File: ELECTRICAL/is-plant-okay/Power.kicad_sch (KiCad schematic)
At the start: 0 parts

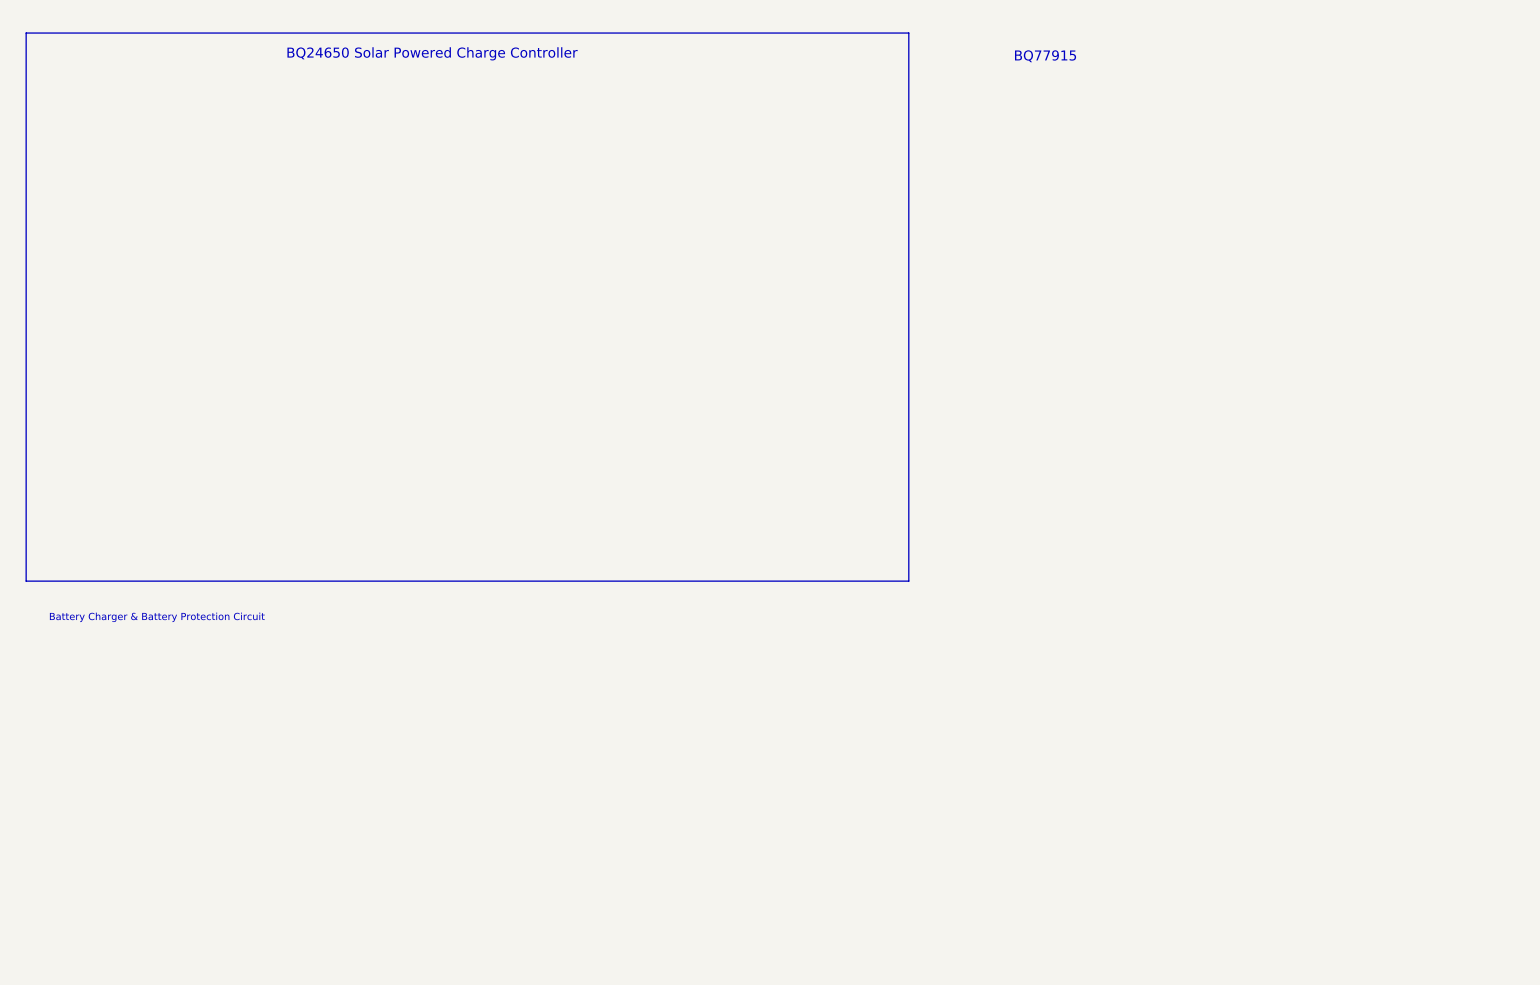
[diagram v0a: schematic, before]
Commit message: add bq24650 schematic
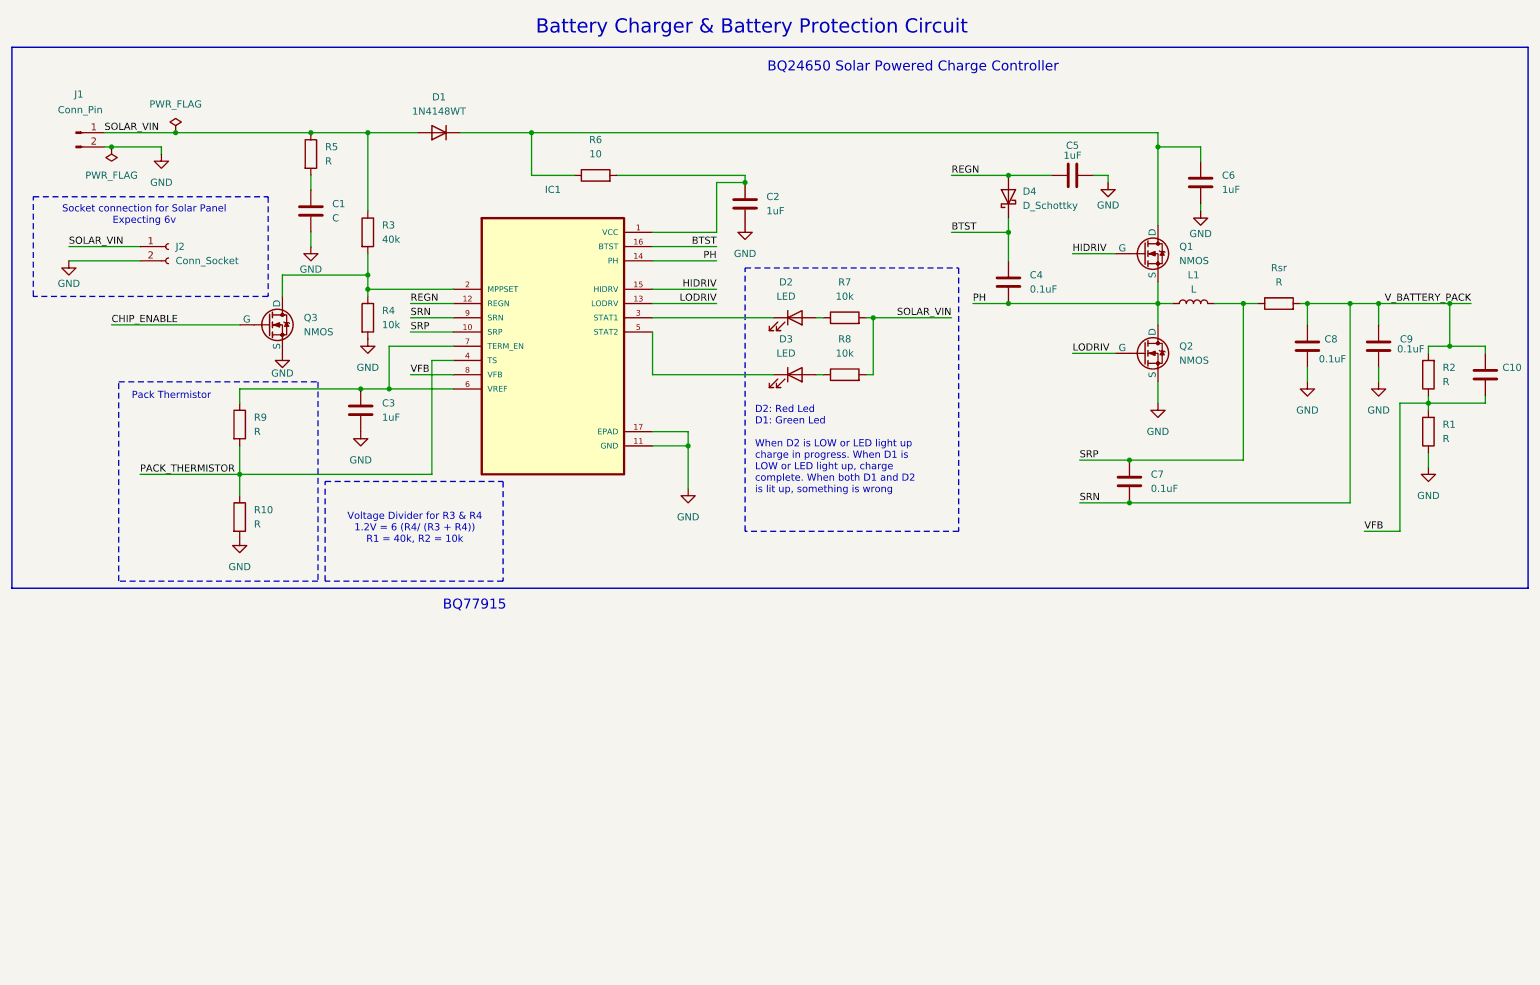
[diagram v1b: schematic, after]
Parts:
- added C1: C, symbol Device:C
- added C10: ~, symbol Device:C
- added C2, C3, C5, C6: 1uF, symbol Device:C
- added C4, C7, C8, C9: 0.1uF, symbol Device:C
- added D1: 1N4148WT, Diode_SMD:D_SOD-523, symbol Diode:1N4148WT
- added D2, D3: LED, symbol Device:LED
- added D4: D_Schottky, symbol Device:D_Schottky
- added IC1: ~, is-plant-okay-foot:QFN50P350X350X100-17N, symbol is-plant-okay-lib:BQ24650RVAT
- added J1: Conn_Pin, symbol Connector:Conn_01x02_Pin
- added J2: Conn_Socket, symbol Connector:Conn_01x02_Socket
- added L1: L, symbol Device:L
- added Q1, Q2, Q3: NMOS, symbol CustomLibrary:NMOS
- added R1, R10, R2, R5, R9, Rsr: R, symbol Device:R
- added R3: 40k, symbol Device:R
- added R4, R7, R8: 10k, symbol Device:R
- added R6: 10, symbol Device:R
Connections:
- new net: C6.1, D1.1 (K), Q1.1 (D), R6.1
- new net: C2.1, IC1.1 (VCC), R6.2
- new net: D3.2 (A), R8.1
- new net: D2.1 (K), IC1.3 (STAT1)
- new net: D2.2 (A), R7.1
- new net: IC1.2 (MPPSET), Q3.1 (D), R3.2, R4.1
- new net: D3.1 (K), IC1.5 (STAT2)
- new net: C3.1, IC1.6 (VREF), IC1.7 (TERM_EN), R9.1
- new net: C1.1, R5.2
- new net BTST: C4.1, D4.1 (K), IC1.16 (BTST)
- new net CHIP_ENABLE: Q3.2 (G)
- new net GND: C1.2, C2.2, C3.2, C5.2, C6.2, C8.2, C9.2, IC1.11 (GND), IC1.17 (EPAD), J1.2 (Pin_2), J2.2 (Pin_2), Q2.3 (S), Q3.3 (S), R1.1, R10.2, R4.2
- new net HIDRIV: IC1.15 (HIDRV), Q1.2 (G)
- new net LODRIV: IC1.13 (LODRV), Q2.2 (G)
- new net PACK_THERMISTOR: IC1.4 (TS), R10.1, R9.2
- new net PH: C4.2, IC1.14 (PH), L1.1, Q1.3 (S), Q2.1 (D)
- new net REGN: C5.1, D4.2 (A), IC1.12 (REGN)
- new net SOLAR_VIN: D1.2 (A), J1.1 (Pin_1), J2.1 (Pin_1), R3.1, R5.1, R7.2, R8.2
- new net SRN: C10.1, C7.2, C8.1, C9.1, IC1.9 (SRN), R2.2, Rsr.2
- new net SRP: C7.1, IC1.10 (SRP), L1.2, Rsr.1
- new net VFB: C10.2, IC1.8 (VFB), R1.2, R2.1
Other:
- note added: "D2: Red Led D1: Green Led When D2 is LOW or LED light up charge in progress. When D1 is LOW or LED light up, charge complete. When both D1 and D2 is lit up, something is wrong"
- note added: "Pack Thermistor"
- note added: "Socket connection for Solar Panel Expecting 6v"
- note added: "Voltage Divider for R3 & R4 1.2V = 6 (R4/ (R3 + R4)) R1 = 40k, R2 = 10k"

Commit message: add bq77915 module
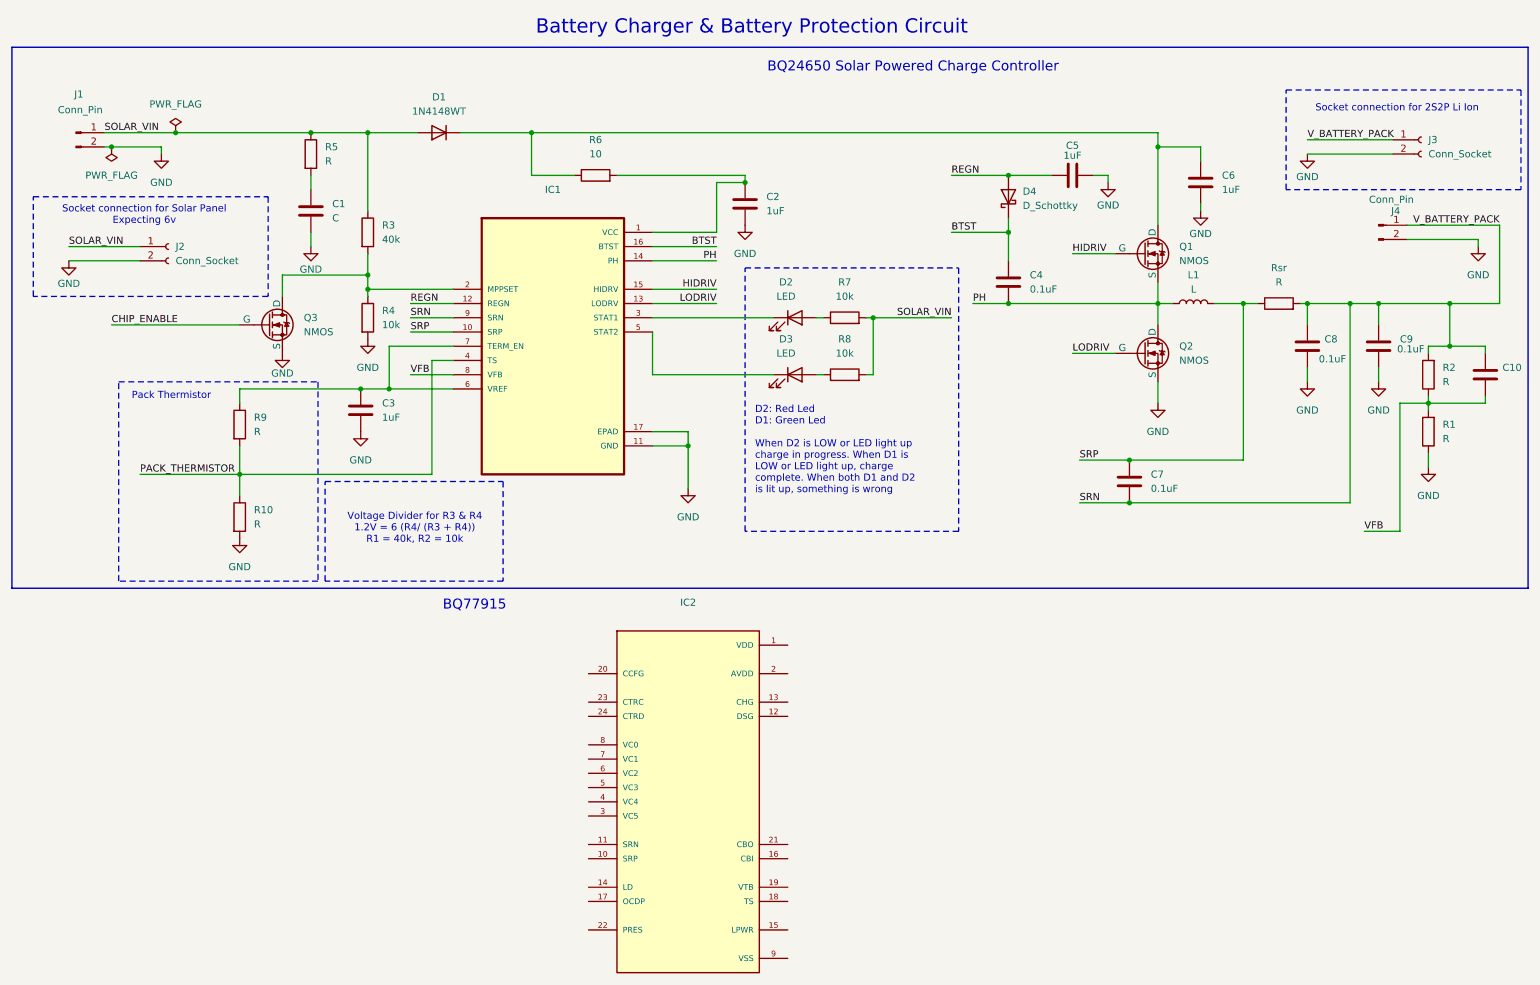
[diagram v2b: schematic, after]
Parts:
- added IC2: ~, is-plant-okay-foot:BQ7791504PW, symbol is-plant-okay-lib:BQ7791504PW
- added J3: Conn_Socket, symbol Connector:Conn_01x02_Socket
- added J4: Conn_Pin, symbol Connector:Conn_01x02_Pin
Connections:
- net GND: now also J3.2 (Pin_2), J4.2 (Pin_2)
- net SRN: now also J3.1 (Pin_1), J4.1 (Pin_1)
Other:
- note added: "Socket connection for 2S2P Li Ion"
